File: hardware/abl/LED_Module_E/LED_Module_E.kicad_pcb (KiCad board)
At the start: 4 copper layers, 140.8 x 26 mm, 98 parts, among them J1 SFW20S-2STE1LF, J3 009159008603906, K1 Conn_01x01, K10 Conn_01x01, K11 Conn_01x01, K12 Conn_01x01, K13 Conn_01x01, K14 Conn_01x01, K15 Conn_01x01, K16 Conn_01x01, K17 Conn_01x01, K18 Conn_01x01, K2 Conn_01x01, K3 Conn_01x01, K4 Conn_01x01, K5 Conn_01x01, K6 Conn_01x01, K7 Conn_01x01, K8 Conn_01x01, K9 Conn_01x01, Q1 Si3456DDV, Q11 Si3456DDV, Q12 Si3456DDV, Q2 Si3456DDV, Q3 Si3456DDV, Q4 Si3456DDV, Q5 Si3456DDV, Q6 Si3456DDV, Q7 Si3456DDV, Q8 Si3456DDV, U2 74HC245, U3 24AA025E48T-I/OT, U4 74LVC1G32

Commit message: Many small adjustments for the next production run.
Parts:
- removed TP1, TP2, TP3, TP4: TestPoint, TestPoint:TestPoint_Pad_D1.0mm
- added H7: MountingHole_Pad, MountingHole:MountingHole_2.5mm_Pad_TopOnly, B.Cu at (160.0, 63.0)
- added H8: MountingHole_Pad, MountingHole:MountingHole_2.5mm_Pad_TopOnly, B.Cu at (115.0, 63.0)
- K1, K10, K11, K12, K13, K14, K15, K16, K17, K18, K2, K3, K4, K5, K6, K7, K8, K9: footprint TestPoint:TestPoint_THTPad_1.0x1.0mm_Drill0.5mm -> TestPoint:TestPoint_THTPad_D1.5mm_Drill0.7mm
- moved K10 10.9 mm to (134.4, 78.0), turned to 0 degrees
- moved K9 8.92 mm to (138.4, 78.0), turned to 0 degrees
- moved K8 8.15 mm to (136.4, 78.0), turned to 0 degrees
- moved K11 6.35 mm to (140.5, 78.0), turned to 0 degrees
- moved K7 5.62 mm to (132.5, 78.0), turned to 0 degrees
- moved K12 5.56 mm to (142.5, 78.0), turned to 0 degrees
- moved K6 4.83 mm to (130.5, 78.0), turned to 0 degrees
- moved K13 4.77 mm to (144.5, 78.0), turned to 0 degrees
- moved K5 4.06 mm to (128.5, 78.0), turned to 0 degrees
- moved K14 4.00 mm to (146.5, 78.0), turned to 0 degrees
- moved K4 3.29 mm to (126.5, 78.0), turned to 0 degrees
- moved K15 3.23 mm to (148.5, 78.0), turned to 0 degrees
- moved K3 2.56 mm to (124.5, 78.0), turned to 0 degrees
- moved K16 2.50 mm to (150.5, 78.0), turned to 0 degrees
- moved K2 1.84 mm to (122.5, 78.0), turned to 0 degrees
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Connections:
- C2 pad 1: +5V -> +4V
- J1 pad 13: +5V -> +4V
- J3 pad 4: +5V -> +4V
- U2 pad 20: +5V -> +4V
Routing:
- net +5V: track 108.1 -> 0.00 mm, vias 4 -> 0
- net /ALERT: track 123.0 -> 94.5 mm, vias 4 -> 2
- net GND: track 31.6 -> 54.9 mm, vias 173 -> 186
- net +3.3V: track 123.0 -> 114.3 mm
- net /SCL: track 70.6 -> 77.0 mm
- net +4V: track 2.98 -> 7.54 mm, vias 72 -> 73
- net /SDA: track 81.7 -> 82.2 mm
- net Net-(R18-Pad2): vias 15 -> 10
- net Net-(R17-Pad2): vias 14 -> 9
- net Net-(R16-Pad2): vias 14 -> 9
- removed copper zone on In1.Cu, net +4V
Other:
- outline, holes or cut-outs redrawn
- board text added: "3.3V"
- board text added: "5V"
- board text added: "AL"
- board text added: "SCL"
- board text added: "SDA"
- board text added: "https://beste-lampe.de"
- board text removed: "+3.3V"
- board text removed: "+5V"
- board text removed: "VLED"
- board text removed: "https://lenaschimmel.de/besteLampe!"

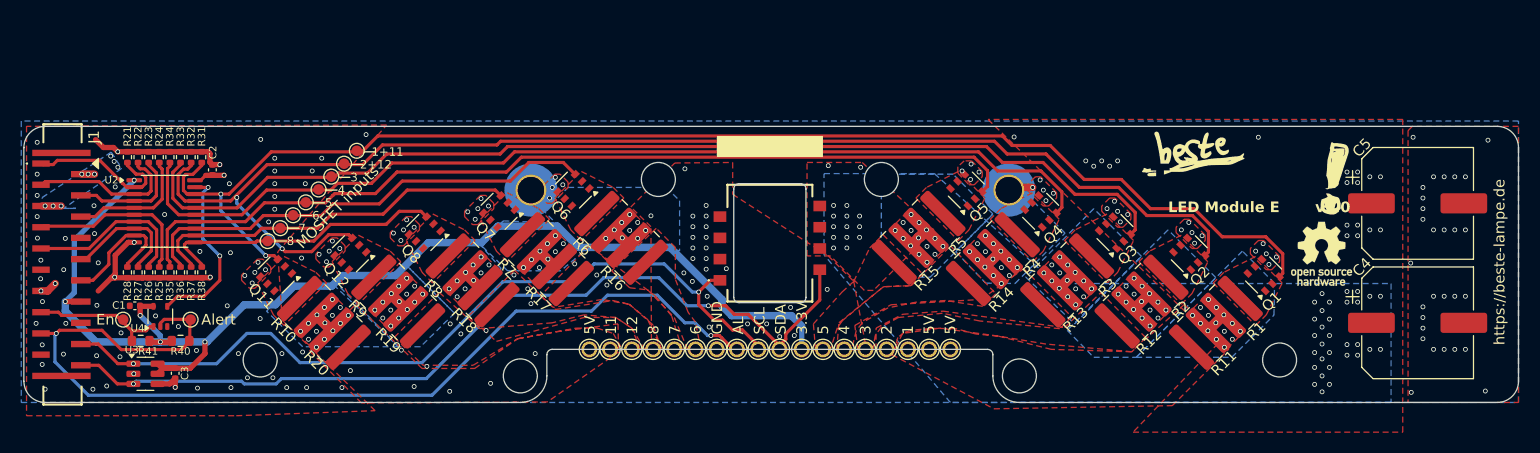
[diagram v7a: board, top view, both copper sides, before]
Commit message: LED Module E version 4.0: two rows of castellated holes instead of one, for larger pitch and easier soldering. Also optimized routing.
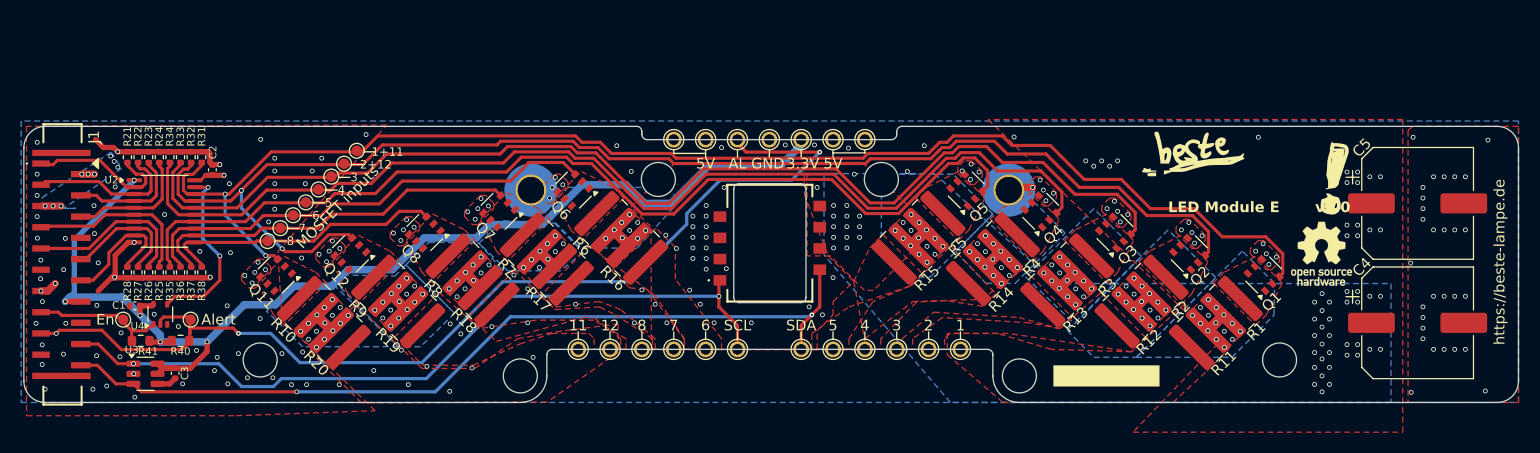
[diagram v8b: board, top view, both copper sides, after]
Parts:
- added K19: Conn_01x01, TestPoint:TestPoint_THTPad_D1.5mm_Drill0.7mm, F.Cu at (128.4, 58.2)
- moved K1 22.6 mm to (131.4, 58.2)
- moved K17 21.7 mm to (143.4, 58.2)
- moved K18 21.3 mm to (146.4, 58.2)
- moved K7 20.4 mm to (137.4, 58.2)
- moved K10 19.8 mm to (134.4, 58.2)
- moved K11 19.8 mm to (140.4, 58.2)
- moved K16 4.95 mm to (155.4, 78.0)
- moved K15 3.95 mm to (152.4, 78.0)
- moved K2 3.00 mm to (119.5, 78.0)
- moved K14 2.95 mm to (149.4, 78.0)
- moved K3 2.05 mm to (122.5, 78.0)
- moved K9 2.05 mm to (140.4, 78.0)
- moved K8 1.95 mm to (134.4, 78.0)
- moved K13 1.95 mm to (146.4, 78.0)
- moved K4 1.05 mm to (125.5, 78.0)
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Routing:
- net Net-(Q3-G): track 101.8 -> 108.9 mm
- net Net-(Q5-G): track 86.4 -> 93.4 mm
- net Net-(Q4-G): track 94.8 -> 101.8 mm
- net +3.3V: track 114.3 -> 109.0 mm
- net /SCL: track 77.0 -> 72.1 mm
- net /ALERT: track 94.5 -> 98.8 mm, vias 2 -> 3
- net Net-(Q12-G): track 123.3 -> 125.6 mm
- net Net-(Q1-G): track 125.3 -> 126.9 mm
- net /SDA: track 82.2 -> 80.7 mm
- net GND: track 54.9 -> 54.0 mm, vias 186 -> 196
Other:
- outline, holes or cut-outs redrawn
- board text added: "LED Module E v4.0"
- board text removed: "LED Module E v3.0"
